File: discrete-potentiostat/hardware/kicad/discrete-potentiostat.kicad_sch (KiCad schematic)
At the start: 69 parts, among them J1 ELECTRODES, J2 SWD, U1 BQ51013BRHLR, U2 MIC5205-3.3YM5, U3 nRF52832-QFAA, U4 OPA2391, U5 REF35102QDBVR, U6 MCP73832T-2ACI/OT, Y1 32MHz 8pF 10ppm

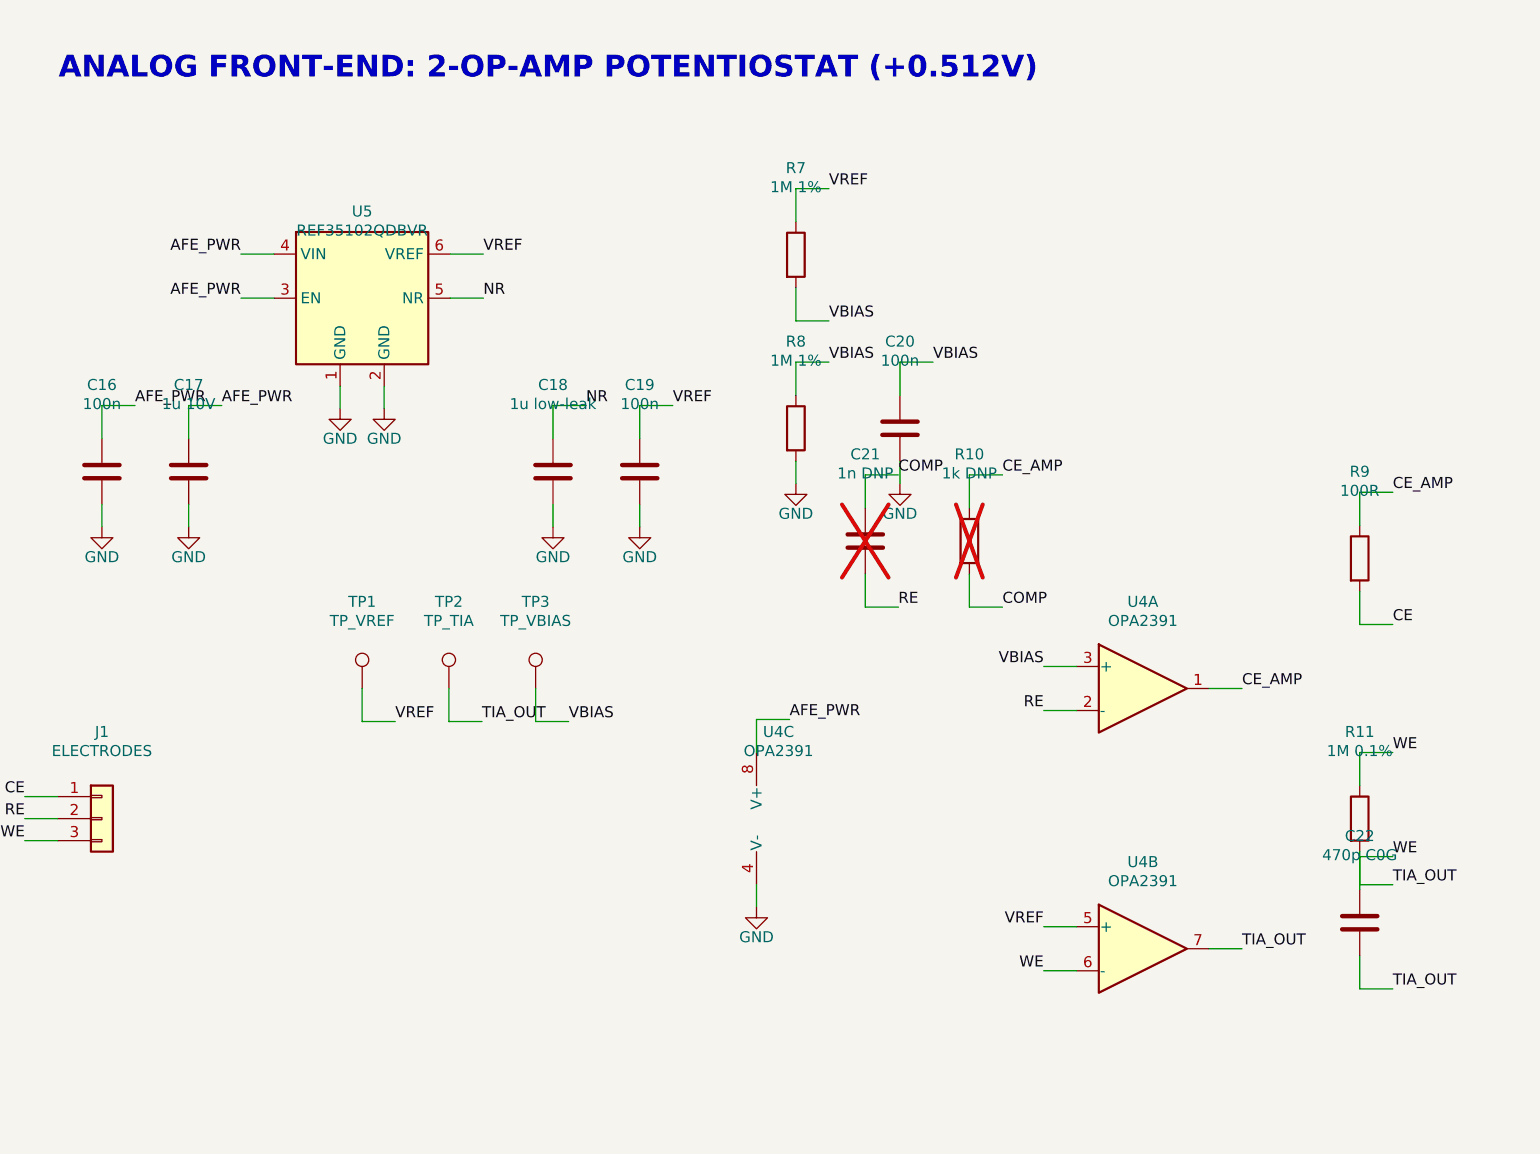
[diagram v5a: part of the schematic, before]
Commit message: Redraw REF35102 and OPA2391 symbols per user's preferred style
- REF35102QDBVR: VIN on top, EN left, VREF/NR right, GND pins 1/2 on the
  bottom (same verified pin numbers, new geometry)
- OPA2391DGKR: single-box dual op amp (A/B triangles inside, inputs left,
  outputs right, V+ top pin 8, V- bottom pin 4) replacing the three-unit
  LM2904-style symbol; one U4 instance carries all 8 pins

Netlist unchanged and re-verified: 47 nets PASS.

Co-Authored-By: Claude Fable 5 <noreply@anthropic.com>
Claude-Session: https://claude.ai/code/session_01GUNJUwfGKqvkZFmTaLQRu3
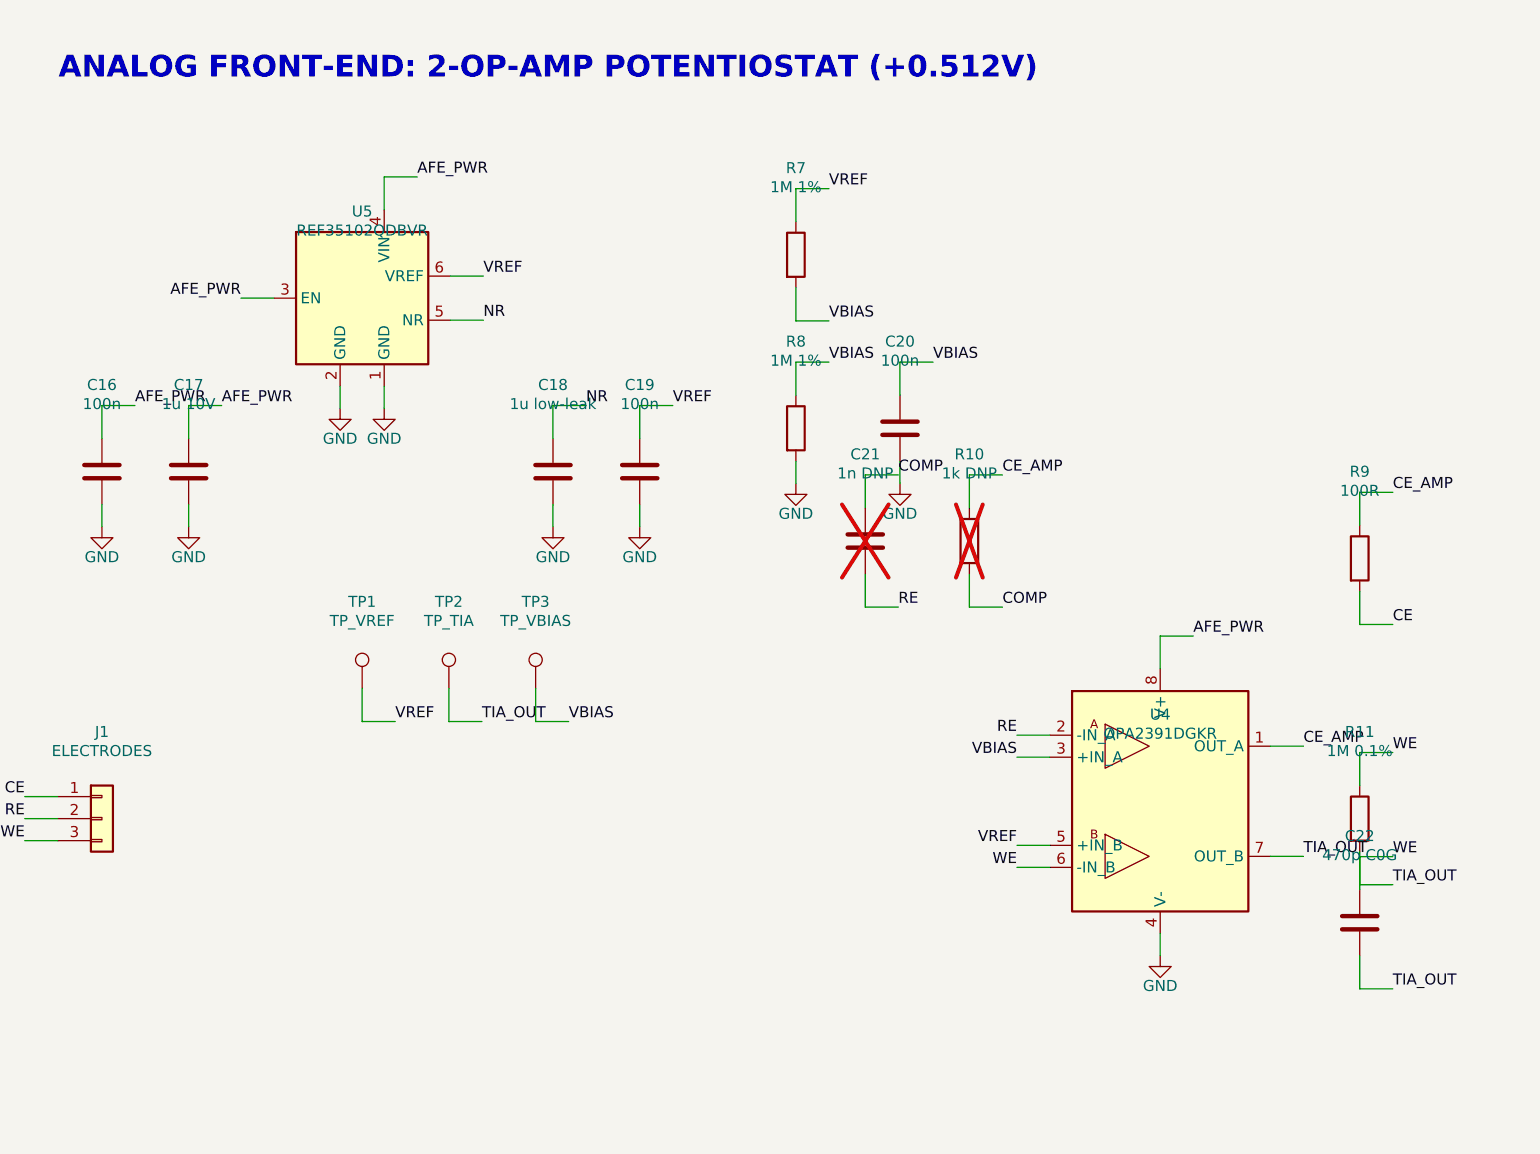
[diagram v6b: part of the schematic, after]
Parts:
- removed U4: OPA2391, Package_SO:VSSOP-8_3.0x3.0mm_P0.65mm, symbol pstat:OPA2391xDGK
- added U4: OPA2391DGKR, Package_SO:VSSOP-8_3.0x3.0mm_P0.65mm, symbol pstat:OPA2391DGKR
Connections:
- net AFE_PWR: now also U4.8 (V+)
- net CE_AMP: now also U4.1 (OUT_A)
- net GND: now also U4.4 (V-)
- net RE: now also U4.2 (-IN_A)
- net TIA_OUT: now also U4.6 (-IN_B), U4.7 (OUT_B)
- net VBIAS: now also U4.3 (+IN_A)
- net VREF: now also U4.5 (+IN_B)

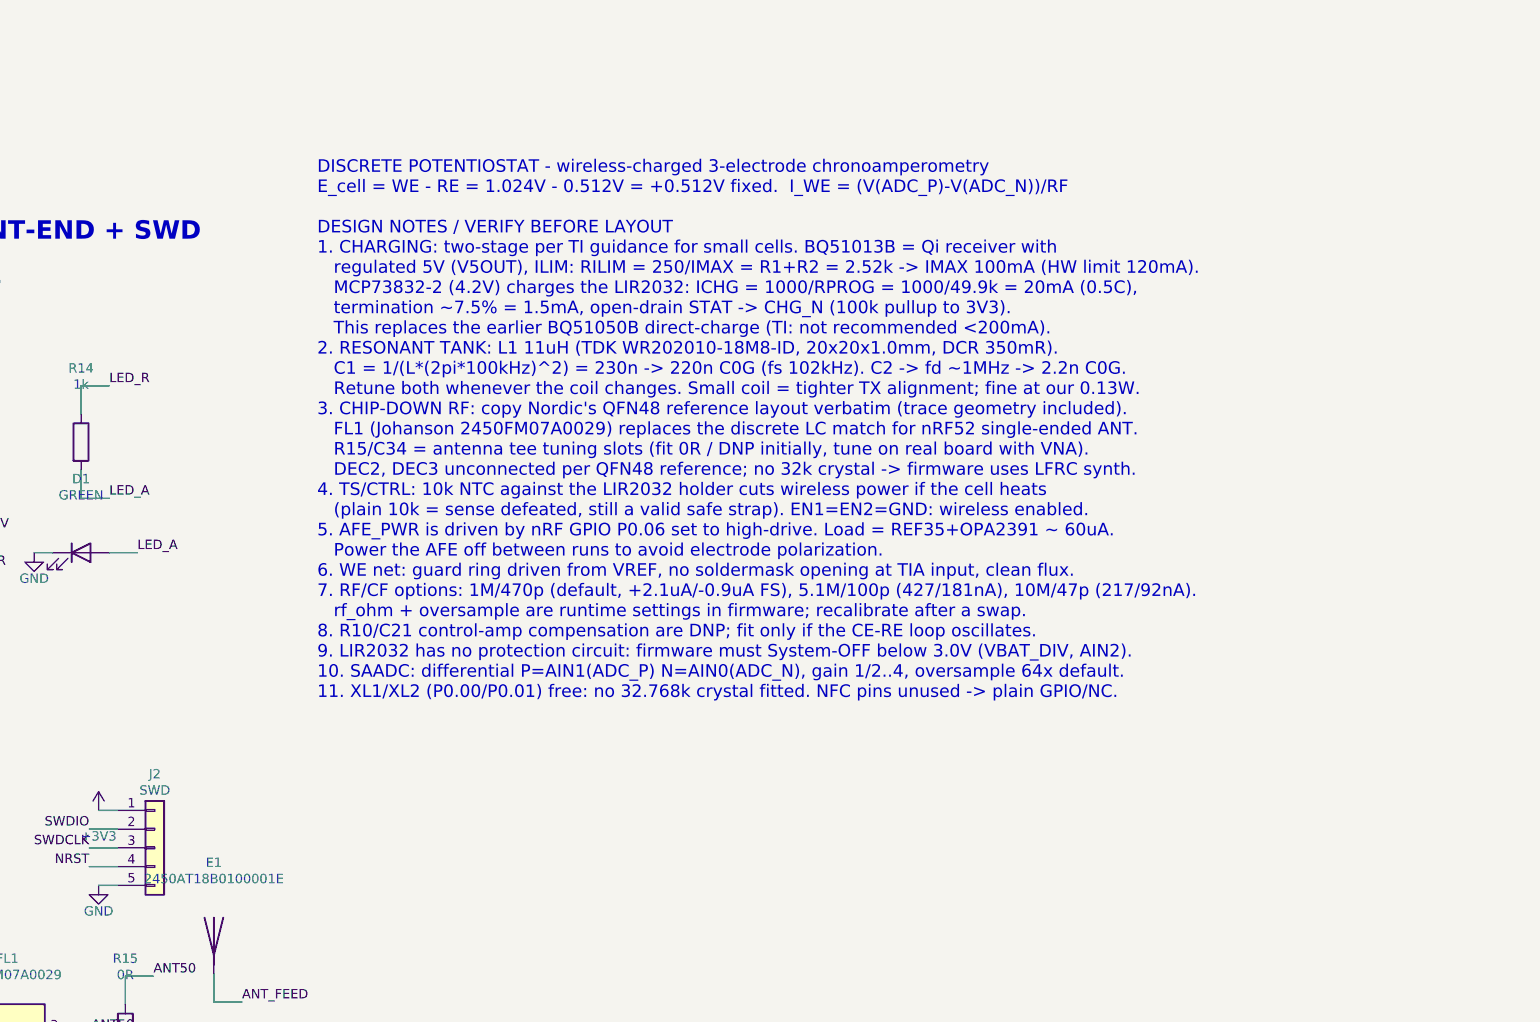
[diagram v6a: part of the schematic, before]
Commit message: Swap chip antenna to Johanson 2450AT07A0100 (0402 micro)
Smallest Johanson 2.4GHz antenna (1.0x0.5x0.37mm). Datasheet ground
keepout must be followed exactly; the existing R15/C34 tee slots handle
on-board tuning. Netlist re-verified (47 nets PASS).

Co-Authored-By: Claude Fable 5 <noreply@anthropic.com>
Claude-Session: https://claude.ai/code/session_01GUNJUwfGKqvkZFmTaLQRu3
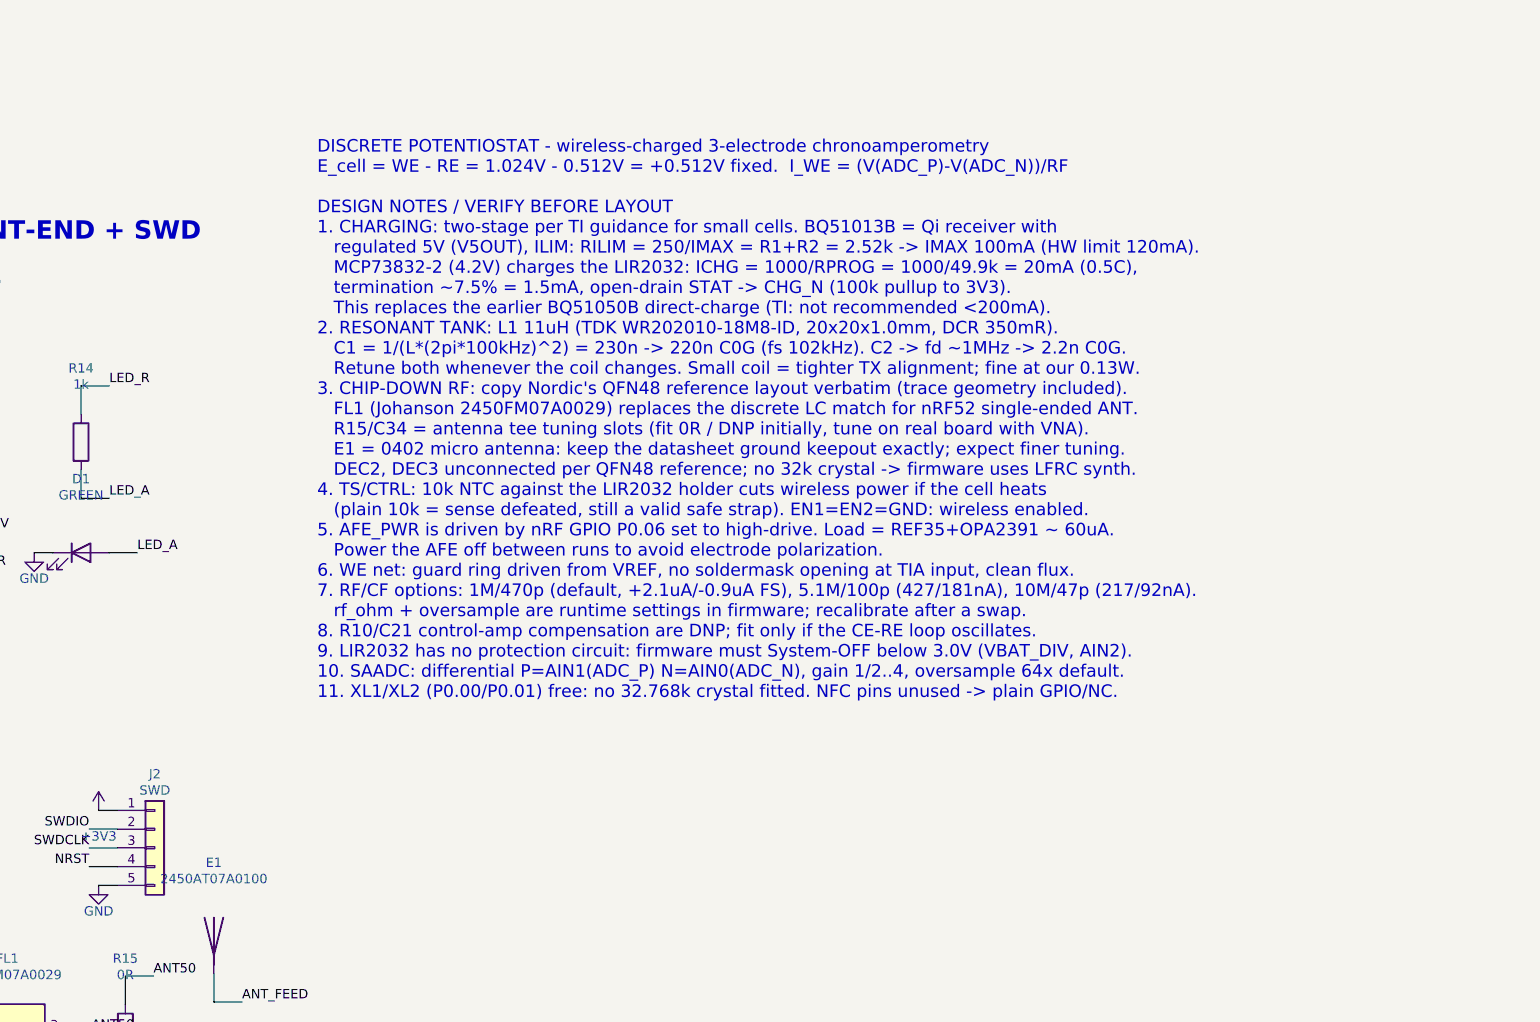
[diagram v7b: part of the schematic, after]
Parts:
- E1: value 2450AT18B0100001E -> 2450AT07A0100; footprint pstat:Johanson_2450AT18B100 -> pstat:Johanson_2450AT07A0100

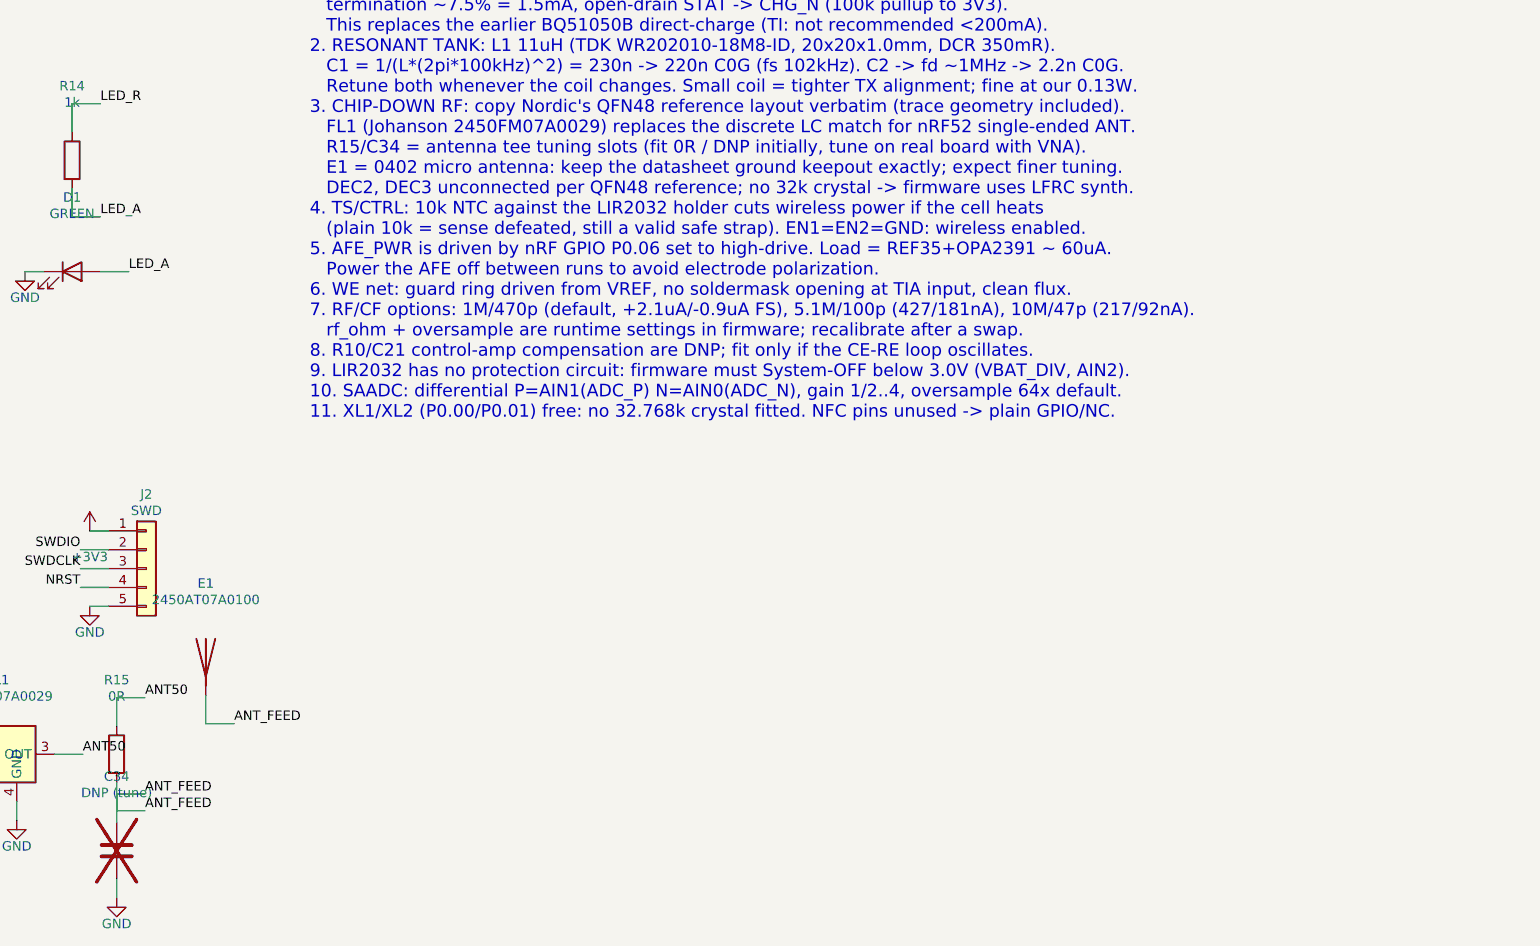
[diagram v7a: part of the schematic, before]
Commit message: Complete antenna tee tuning network (series-shunt-series per Johanson)
Adds R16 (0R) after the C34 shunt slot so the full tee recommended by
Johanson is available for on-board antenna tuning. Radio-side matching
needs no discrete LC: FL1 (2450FM07A0029) is the complete impedance
match + harmonic LPF for the nRF52832 ANT output. Netlist PASS.

Co-Authored-By: Claude Fable 5 <noreply@anthropic.com>
Claude-Session: https://claude.ai/code/session_01GUNJUwfGKqvkZFmTaLQRu3
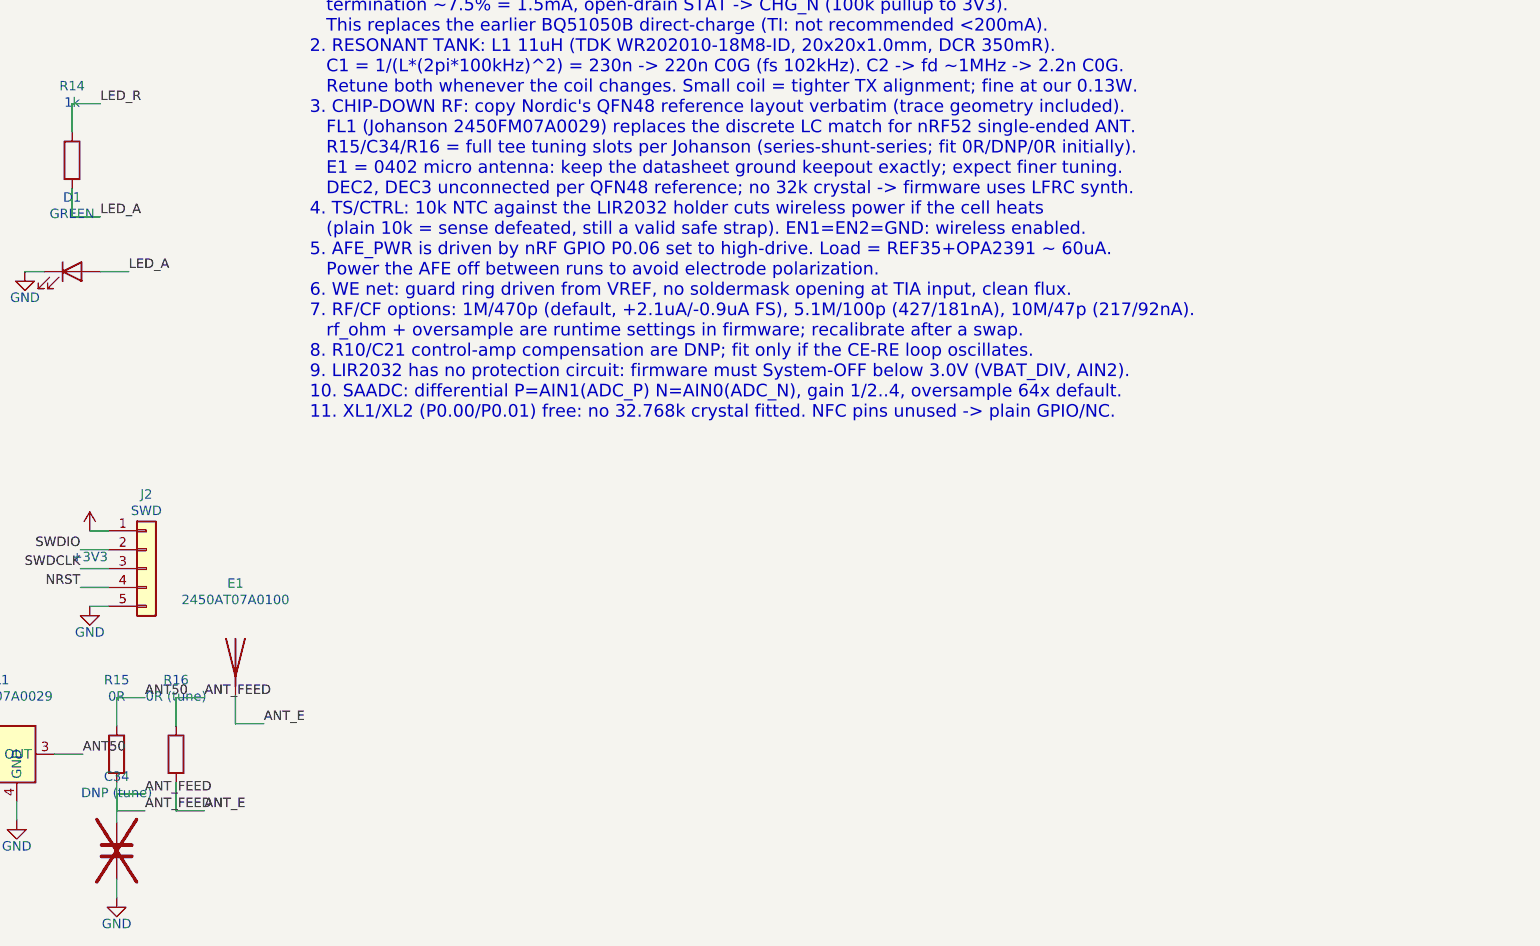
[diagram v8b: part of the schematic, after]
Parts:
- added R16: 0R (tune), Resistor_SMD:R_0402_1005Metric, symbol Device:R
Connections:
- net ANT_FEED: now also R16.1; no longer E1.1 (A)
- new net ANT_E: E1.1 (A), R16.2
